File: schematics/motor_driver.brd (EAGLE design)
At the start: 39 x 36 mm, 15 parts

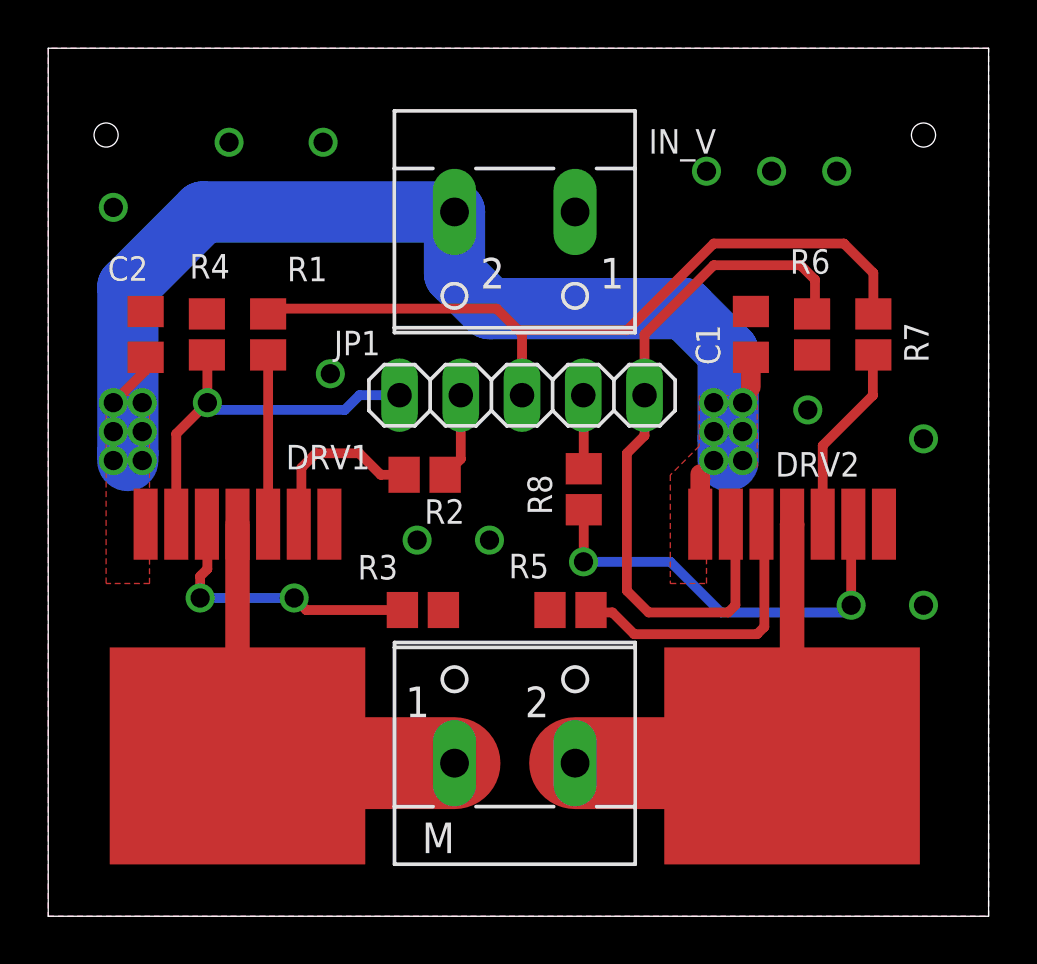
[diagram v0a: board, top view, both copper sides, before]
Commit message: Added a common ground for the driver.
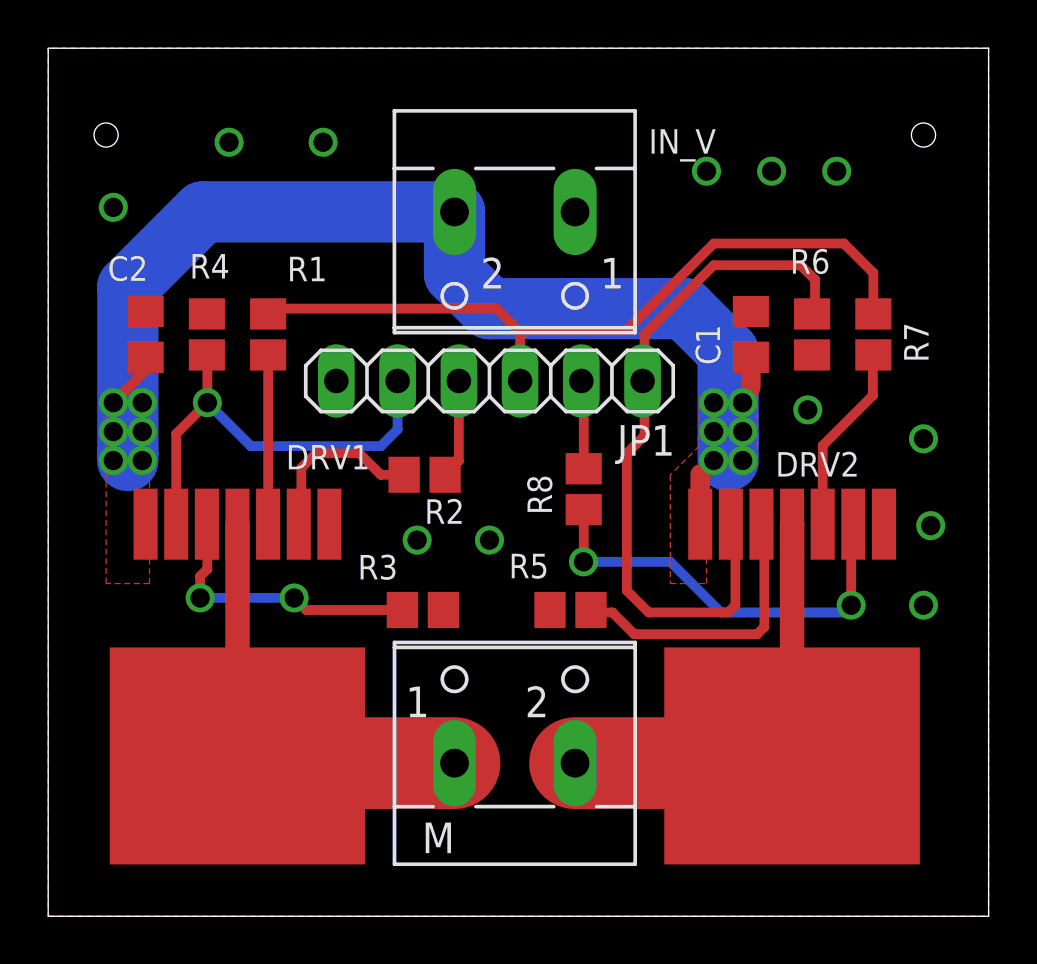
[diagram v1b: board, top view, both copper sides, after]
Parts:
- JP1: device pinhead:1X05 -> pinhead:1X06
- moved JP1 1.47 mm to (18.3, 22.2)
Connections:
- net GND: now also JP1.6
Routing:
- net N$5: track 15.9 -> 18.9 mm
- net IN_R: track 3.06 -> 3.68 mm
- net IN_L: track 3.57 -> 4.13 mm
- net /INH: track 32.0 -> 31.5 mm
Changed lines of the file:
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@@
 <attribute name="NAME" x="15.5038" y="2.6162" size="1.27" layer="25" ratio="10"/>
 </element>
-<element name="JP1" library="pinhead" package="1X05" value="" x="19.65" y="21.61" smashed="yes" rot="R180">
-<attribute name="NAME" x="13.7762" y="24.2812" size="1.016" layer="25" ratio="10" rot="R180"/>
-<attribute name="VALUE" x="26" y="24.785" size="1.27" layer="27" rot="R180"/>
-</element>
+<element name="JP1" library="pinhead" package="1X06" value="" x="18.3" y="22.2" rot="R180"/>
 </elements>
 <signals>
@@
 <via x="2.7" y="29.4" extent="1-16" drill="0.8"/>
 <via x="36.3" y="19.8" extent="1-16" drill="0.8"/>
-<via x="11.7" y="22.5" extent="1-16" drill="0.8"/>
+<via x="36.6" y="16.2" extent="1-16" drill="0.8"/>
 <polygon width="0.4064" layer="1" rank="3">
 <vertex x="0" y="36"/>
@@
 </polygon>
 <via x="36.3" y="12.9" extent="1-16" drill="0.8"/>
+<contactref element="JP1" pad="6"/>
 </signal>
 <signal name="/INH">
 <contactref element="R1" pad="1"/>
 <contactref element="R7" pad="2"/>
-<contactref element="JP1" pad="3"/>
-<wire x1="19.65" y1="21.61" x2="19.65" y2="24.15" width="0.4064" layer="1"/>
 <wire x1="19.65" y1="24.15" x2="19.5" y2="24.3" width="0.4064" layer="1"/>
 <wire x1="19.5" y1="24.3" x2="18.6" y2="25.2" width="0.4064" layer="1"/>
@@
 <wire x1="34.22" y1="26.68" x2="33" y2="27.9" width="0.4064" layer="1"/>
 <wire x1="33" y1="27.9" x2="27.6" y2="27.9" width="0.4064" layer="1"/>
+<contactref element="JP1" pad="3"/>
+<wire x1="19.57" y1="22.2" x2="19.57" y2="24.07" width="0.4064" layer="1"/>
+<wire x1="19.57" y1="24.07" x2="19.65" y2="24.15" width="0.4064" layer="1"/>
 </signal>
 <signal name="IN_L">
 <contactref element="R2" pad="1"/>
 <contactref element="JP1" pad="4"/>
-<wire x1="17.11" y1="21.61" x2="17.11" y2="18.96" width="0.4064" layer="1"/>
-<wire x1="17.11" y1="18.96" x2="16.46" y2="18.31" width="0.4064" layer="1"/>
+<wire x1="17.03" y1="22.2" x2="17.03" y2="18.88" width="0.4064" layer="1"/>
+<wire x1="17.03" y1="18.88" x2="16.46" y2="18.31" width="0.4064" layer="1"/>
 </signal>
 <signal name="N$5">
 <contactref element="R4" pad="1"/>
 <contactref element="DRV1" pad="6"/>
-<contactref element="JP1" pad="5"/>
 <wire x1="5.31" y1="16.26" x2="5.31" y2="20.01" width="0.4064" layer="1"/>
 <wire x1="6.6" y1="21.3" x2="6.6" y2="23.26" width="0.4064" layer="1"/>
@@
 <via x="6.6" y="21.3" extent="1-16" drill="0.8"/>
 <wire x1="5.31" y1="20.01" x2="6.6" y2="21.3" width="0.4064" layer="1"/>
-<wire x1="14.57" y1="21.61" x2="12.91" y2="21.61" width="0.4064" layer="16"/>
-<wire x1="12.91" y1="21.61" x2="12.3" y2="21" width="0.4064" layer="16"/>
-<wire x1="12.3" y1="21" x2="6.9" y2="21" width="0.4064" layer="16"/>
 <wire x1="6.9" y1="21" x2="6.6" y2="21.3" width="0.4064" layer="16"/>
+<contactref element="JP1" pad="5"/>
+<wire x1="14.49" y1="22.2" x2="14.49" y2="20.19" width="0.4064" layer="16"/>
+<wire x1="14.49" y1="20.19" x2="13.8" y2="19.5" width="0.4064" layer="16"/>
+<wire x1="13.8" y1="19.5" x2="8.4" y2="19.5" width="0.4064" layer="16"/>
+<wire x1="8.4" y1="19.5" x2="6.6" y2="21.3" width="0.4064" layer="16"/>
 </signal>
 <signal name="N$6">
@@
 </signal>
 <signal name="N$10">
-<contactref element="JP1" pad="1"/>
 <contactref element="DRV2" pad="6"/>
 <contactref element="R6" pad="2"/>
-<wire x1="24.73" y1="21.61" x2="24.73" y2="24.13" width="0.4064" layer="1"/>
 <wire x1="24.73" y1="24.13" x2="27.6" y2="27" width="0.4064" layer="1"/>
 <wire x1="27.6" y1="27" x2="31.2" y2="27" width="0.4064" layer="1"/>
@@
 <wire x1="28.5" y1="12.9" x2="28.5" y2="16.07" width="0.4064" layer="1"/>
 <wire x1="28.5" y1="16.07" x2="28.31" y2="16.26" width="0.4064" layer="1"/>
-<wire x1="24.73" y1="21.61" x2="24.73" y2="19.93" width="0.4064" layer="1"/>
 <wire x1="24.73" y1="19.93" x2="24" y2="19.2" width="0.4064" layer="1"/>
 <wire x1="24" y1="19.2" x2="24" y2="13.5" width="0.4064" layer="1"/>
@@
 <wire x1="24.9" y1="12.6" x2="28.2" y2="12.6" width="0.4064" layer="1"/>
 <wire x1="28.2" y1="12.6" x2="28.5" y2="12.9" width="0.4064" layer="1"/>
+<contactref element="JP1" pad="1"/>
+<wire x1="24.73" y1="19.93" x2="24.73" y2="22.12" width="0.4064" layer="1"/>
+<wire x1="24.73" y1="22.12" x2="24.65" y2="22.2" width="0.4064" layer="1"/>
+<wire x1="24.73" y1="24.13" x2="24.73" y2="22.28" width="0.4064" layer="1"/>
+<wire x1="24.73" y1="22.28" x2="24.65" y2="22.2" width="0.4064" layer="1"/>
 </signal>
 <signal name="N$11">
@@
 <contactref element="R8" pad="2"/>
 <contactref element="JP1" pad="2"/>
-<wire x1="22.21" y1="18.56" x2="22.21" y2="21.59" width="0.4064" layer="1"/>
-<wire x1="22.21" y1="21.59" x2="22.19" y2="21.61" width="0.4064" layer="1"/>
+<wire x1="22.21" y1="18.56" x2="22.21" y2="22.1" width="0.4064" layer="1"/>
+<wire x1="22.21" y1="22.1" x2="22.11" y2="22.2" width="0.4064" layer="1"/>
 </signal>
 </signals>

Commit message: Added extra supply caps.
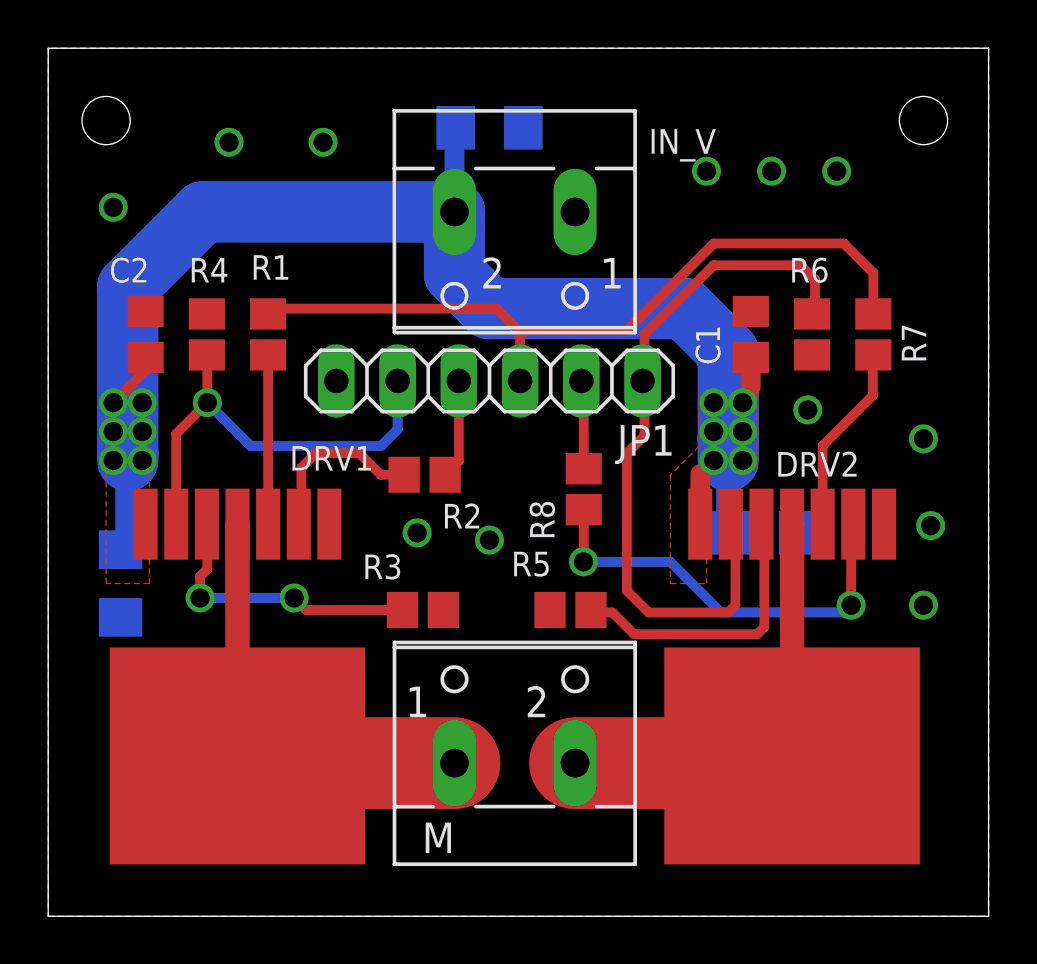
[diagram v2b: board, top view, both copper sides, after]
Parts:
- added C3, C4, C5: 10uF, resistor:C1206
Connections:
- net GND: now also C3.2, C4.2, C5.2
- net VSS: now also C3.1, C4.1, C5.1
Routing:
- net VSS: track 49.8 -> 61.1 mm
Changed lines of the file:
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@@
 <layer number="25" name="tNames" color="7" fill="1" visible="yes" active="yes"/>
 <layer number="26" name="bNames" color="7" fill="1" visible="yes" active="yes"/>
-<layer number="27" name="tValues" color="7" fill="1" visible="no" active="yes"/>
+<layer number="27" name="tValues" color="7" fill="1" visible="yes" active="yes"/>
 <layer number="28" name="bValues" color="7" fill="1" visible="yes" active="yes"/>
 <layer number="29" name="tStop" color="7" fill="3" visible="no" active="yes"/>
@@
 <wire x1="39" y1="36" x2="0" y2="36" width="0" layer="20"/>
 <wire x1="0" y1="36" x2="0" y2="0" width="0" layer="20"/>
-<hole x="2.4" y="32.4" drill="1"/>
-<hole x="36.3" y="32.4" drill="1"/>
+<hole x="2.4" y="33" drill="2"/>
+<hole x="36.3" y="33" drill="2"/>
 </plain>
 <attributes>
@@
 <element name="DRV1" library="rvp" package="TO-263-8" value="FAN7093_F085SMD" x="7.85" y="6.65" smashed="yes" rot="R180">
 <attribute name="FAN7093_F085" value="" x="-11.2" y="18.08" size="1.778" layer="27" rot="R180" display="off"/>
-<attribute name="NAME" x="13.35" y="19.55" size="1.016" layer="25" font="vector" rot="R180"/>
+<attribute name="NAME" x="13.5" y="19.5" size="1.016" layer="25" font="vector" rot="R180"/>
 </element>
 <element name="DRV2" library="rvp" package="TO-263-8" value="FAN7093_F085SMD" x="30.85" y="6.65" smashed="yes" rot="R180">
@@
 </element>
 <element name="R1" library="resistor" package="R0805" value="10k" x="9.12" y="24.13" smashed="yes" rot="R270">
-<attribute name="NAME" x="9.908" y="26.336" size="1.016" layer="25"/>
-<attribute name="VALUE" x="6.834" y="24.892" size="1.27" layer="27" rot="R270"/>
+<attribute name="NAME" x="8.4" y="26.4" size="1.016" layer="25"/>
+<attribute name="VALUE" x="8.4" y="27.6" size="1.016" layer="27"/>
 </element>
 <element name="R2" library="resistor" package="R0805" value="10k" x="15.61" y="18.31" smashed="yes" rot="R180">
-<attribute name="NAME" x="17.272" y="17.294" size="1.016" layer="25" rot="R180"/>
-<attribute name="VALUE" x="16.372" y="20.596" size="1.27" layer="27" rot="R180"/>
+<attribute name="NAME" x="18" y="17.1" size="1.016" layer="25" rot="R180"/>
+<attribute name="VALUE" x="15" y="17.4" size="1.016" layer="27" rot="R180"/>
 </element>
 <element name="R3" library="resistor" package="R0805" value="510" x="15.54" y="12.7" smashed="yes" rot="R180">
-<attribute name="NAME" x="14.502" y="14.984" size="1.016" layer="25" rot="R180"/>
-<attribute name="VALUE" x="16.302" y="14.986" size="1.27" layer="27" rot="R180"/>
+<attribute name="NAME" x="14.7" y="15" size="1.016" layer="25" rot="R180"/>
+<attribute name="VALUE" x="17.4" y="15" size="1.016" layer="27" rot="R180"/>
 </element>
 <element name="R4" library="resistor" package="R0805" value="1k" x="6.58" y="24.13" smashed="yes" rot="R90">
-<attribute name="NAME" x="7.532" y="27.464" size="1.016" layer="25" rot="R180"/>
-<attribute name="VALUE" x="8.866" y="23.368" size="1.27" layer="27" rot="R90"/>
+<attribute name="NAME" x="7.5" y="27.3" size="1.016" layer="25" rot="R180"/>
+<attribute name="VALUE" x="7.532" y="28.666" size="1.016" layer="27" rot="R180"/>
 </element>
 <element name="R5" library="resistor" package="R0805" value="510" x="21.66" y="12.7" smashed="yes">
-<attribute name="NAME" x="19.098" y="14.016" size="1.016" layer="25"/>
-<attribute name="VALUE" x="20.898" y="10.414" size="1.27" layer="27"/>
+<attribute name="NAME" x="19.2" y="14.1" size="1.016" layer="25"/>
+<attribute name="VALUE" x="20.7" y="11.1" size="1.016" layer="27" rot="R180"/>
 </element>
 <element name="R6" library="resistor" package="R0805" value="1k" x="31.68" y="24.13" smashed="yes" rot="R90">
-<attribute name="NAME" x="32.432" y="27.664" size="1.016" layer="25" rot="R180"/>
-<attribute name="VALUE" x="33.966" y="23.368" size="1.27" layer="27" rot="R90"/>
+<attribute name="NAME" x="32.4" y="27.3" size="1.016" layer="25" rot="R180"/>
+<attribute name="VALUE" x="32.1" y="28.8" size="1.27" layer="27" rot="R180"/>
 </element>
 <element name="R7" library="resistor" package="R0805" value="10k" x="34.22" y="24.13" smashed="yes" rot="R90">
-<attribute name="NAME" x="35.496" y="24.632" size="1.016" layer="25" rot="R270"/>
-<attribute name="VALUE" x="36.506" y="23.368" size="1.27" layer="27" rot="R90"/>
+<attribute name="NAME" x="35.4" y="24.6" size="1.016" layer="25" rot="R270"/>
+<attribute name="VALUE" x="36.3" y="24.9" size="1.016" layer="27" rot="R90"/>
 </element>
 <element name="R8" library="resistor" package="R0805" value="10k" x="22.21" y="17.71" smashed="yes" rot="R90">
-<attribute name="NAME" x="20.894" y="16.648" size="1.016" layer="25" rot="R90"/>
-<attribute name="VALUE" x="24.496" y="16.948" size="1.27" layer="27" rot="R90"/>
+<attribute name="NAME" x="21" y="15.6" size="1.016" layer="25" rot="R90"/>
+<attribute name="VALUE" x="21" y="17.7" size="1.016" layer="27" rot="R90"/>
 </element>
 <element name="C1" library="rcl" package="C0805" value="470nF" x="29.14" y="24.13" smashed="yes" rot="R90">
 <attribute name="NAME" x="27.87" y="22.86" size="1.016" layer="25" rot="R90"/>
-<attribute name="VALUE" x="31.68" y="22.86" size="1.27" layer="27" rot="R90"/>
+<attribute name="VALUE" x="27.6" y="24.9" size="1.016" layer="27" rot="R90"/>
 </element>
 <element name="C2" library="rcl" package="C0805" value="470nF" x="4.04" y="24.13" smashed="yes" rot="R90">
-<attribute name="NAME" x="4.14" y="27.37" size="1.016" layer="25" rot="R180"/>
-<attribute name="VALUE" x="6.58" y="22.86" size="1.27" layer="27" rot="R90"/>
+<attribute name="NAME" x="4.2" y="27.3" size="1.016" layer="25" rot="R180"/>
+<attribute name="VALUE" x="5.7" y="28.5" size="1.016" layer="27" rot="R180"/>
 </element>
 <element name="IN_V" library="con-wago-500" package="W237-102" value="" x="19.35" y="27.94" smashed="yes" rot="R180">
@@
 </element>
 <element name="JP1" library="pinhead" package="1X06" value="" x="18.3" y="22.2" rot="R180"/>
+<element name="C3" library="resistor" package="C1206" value="10uF" x="18.3" y="32.7" smashed="yes" rot="MR180">
+<attribute name="NAME" x="15" y="31.5" size="1.016" layer="26" rot="MR0"/>
+<attribute name="VALUE" x="15.3" y="33.3" size="1.016" layer="28" rot="MR0"/>
+</element>
+<element name="C4" library="resistor" package="C1206" value="10uF" x="3" y="13.8" smashed="yes" rot="MR270">
+<attribute name="NAME" x="1.8" y="10.8" size="1.016" layer="26" rot="MR180"/>
+<attribute name="VALUE" x="1.8" y="9" size="1.016" layer="28" rot="MR180"/>
+</element>
+<element name="C5" library="resistor" package="C1206" value="10uF" x="29.7" y="15.9" smashed="yes" rot="MR180">
+<attribute name="NAME" x="32.4" y="15.9" size="1.016" layer="26" rot="MR180"/>
+<attribute name="VALUE" x="32.4" y="17.4" size="1.016" layer="28" rot="MR180"/>
+</element>
 </elements>
 <signals>
@@
 <contactref element="R6" pad="1"/>
 <via x="31.5" y="21" extent="1-16" drill="0.8"/>
-<via x="15.3" y="15.6" extent="1-16" drill="0.8"/>
+<via x="15.3" y="15.9" extent="1-16" drill="0.8"/>
 <via x="18.3" y="15.6" extent="1-16" drill="0.8"/>
 <via x="7.5" y="32.1" extent="1-16" drill="0.8"/>
@@
 <via x="36.3" y="12.9" extent="1-16" drill="0.8"/>
 <contactref element="JP1" pad="6"/>
+<contactref element="C3" pad="2"/>
+<contactref element="C4" pad="2"/>
+<contactref element="C5" pad="2"/>
 </signal>
 <signal name="/INH">
@@
 <wire x1="16.85" y1="29.21" x2="6.41" y2="29.21" width="2.54" layer="16"/>
 <wire x1="6.41" y1="29.21" x2="3.3" y2="26.1" width="2.54" layer="16"/>
-<wire x1="16.85" y1="29.21" x2="16.85" y2="26.65" width="2.54" layer="16"/>
+<wire x1="16.85" y1="29.21" x2="16.85" y2="28.5" width="2.54" layer="16"/>
+<wire x1="16.85" y1="28.5" x2="16.85" y2="26.65" width="2.54" layer="16"/>
 <wire x1="16.85" y1="26.65" x2="18.3" y2="25.2" width="2.54" layer="16"/>
 <wire x1="18.3" y1="25.2" x2="26.4" y2="25.2" width="2.54" layer="16"/>
@@
 <wire x1="27.6" y1="20.1" x2="27.9" y2="20.1" width="0.4064" layer="16"/>
 <wire x1="27.9" y1="20.1" x2="28.2" y2="19.8" width="0.4064" layer="16"/>
+<contactref element="C3" pad="1"/>
+<wire x1="16.9" y1="32.7" x2="16.85" y2="32.7" width="0.8128" layer="16"/>
+<wire x1="16.85" y1="32.7" x2="16.85" y2="28.5" width="0.8128" layer="16"/>
+<contactref element="C4" pad="1"/>
+<contactref element="C5" pad="1"/>
+<wire x1="28.3" y1="15.9" x2="28.2" y2="15.9" width="0.8128" layer="16"/>
+<wire x1="3" y1="15.2" x2="3.3" y2="15.2" width="0.8128" layer="16"/>
+<wire x1="3.3" y1="15.2" x2="3.3" y2="18.9" width="1.016" layer="16"/>
+<wire x1="28.2" y1="15.9" x2="28.2" y2="18.9" width="1.016" layer="16"/>
 </signal>
 <signal name="N$8">

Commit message: Added names to unnamed signals.
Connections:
- net N$10 renamed IS_R
- net N$5 renamed IS_L
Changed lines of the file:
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@@
 <wire x1="17.03" y1="18.88" x2="16.46" y2="18.31" width="0.4064" layer="1"/>
 </signal>
-<signal name="N$5">
+<signal name="IS_L">
 <contactref element="R4" pad="1"/>
 <contactref element="DRV1" pad="6"/>
@@
 <wire x1="22.61" y1="12.6" x2="22.51" y2="12.7" width="0.4064" layer="1"/>
 </signal>
-<signal name="N$10">
+<signal name="IS_R">
 <contactref element="DRV2" pad="6"/>
 <contactref element="R6" pad="2"/>
